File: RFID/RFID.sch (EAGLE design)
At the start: 2 parts, among them IC1 ARDUINO_PRO_MICRO, IC2 RFID_SENSOR

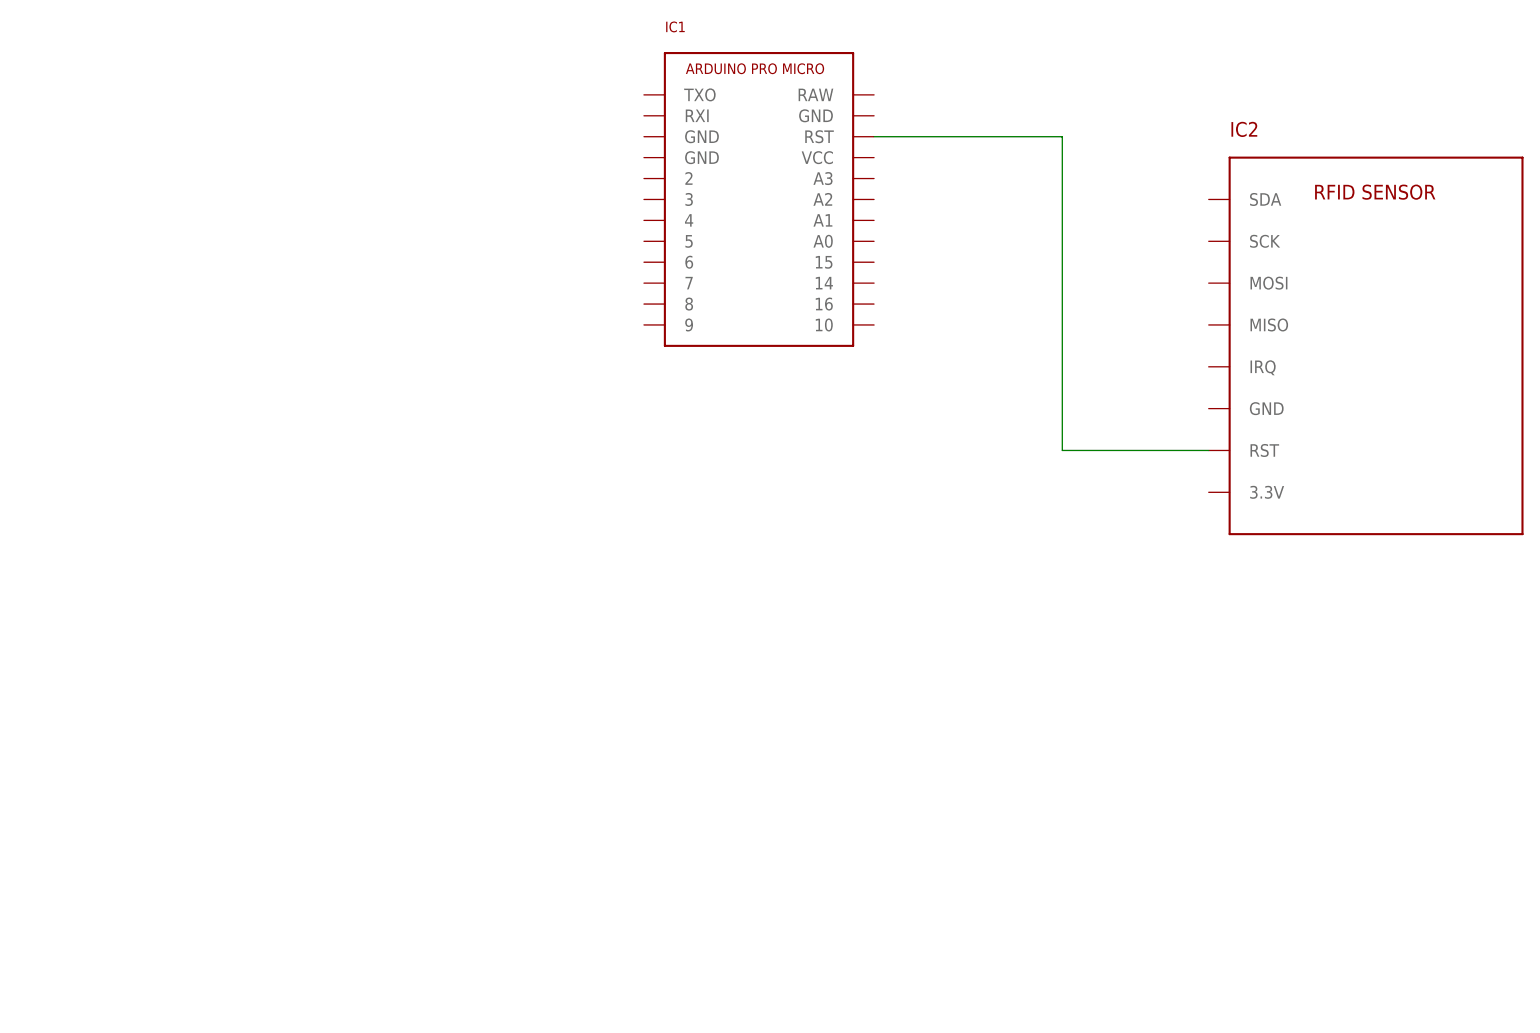
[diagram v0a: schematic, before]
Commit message: Remove old RFID board
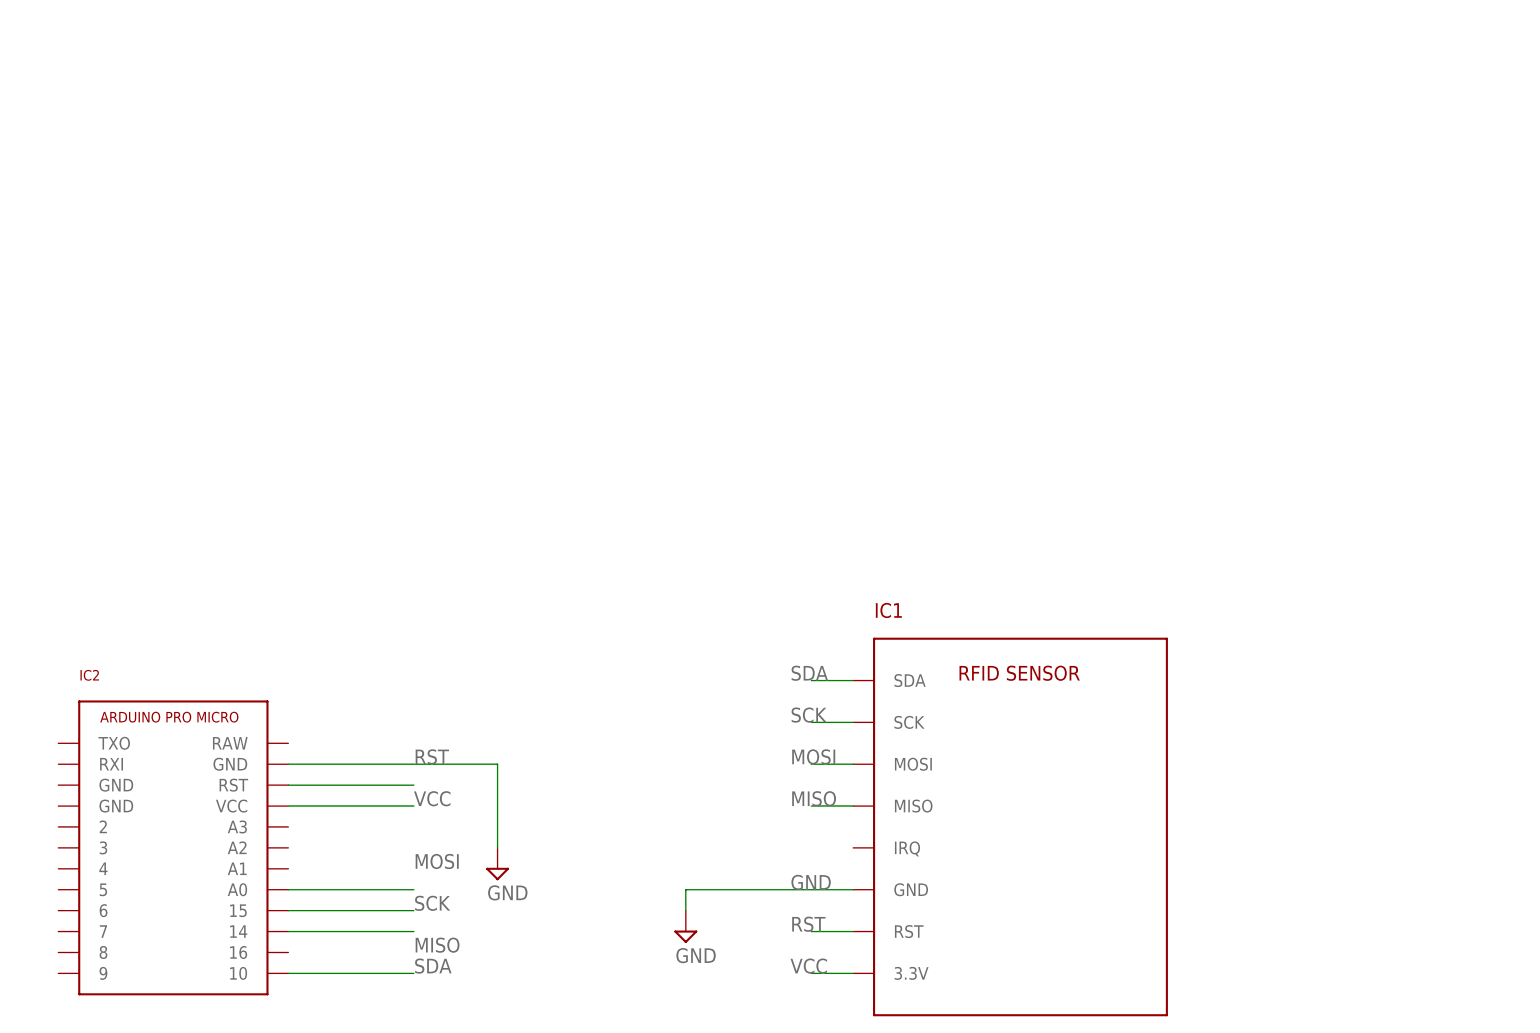
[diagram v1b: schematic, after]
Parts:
- IC1: value ARDUINO_PRO_MICRO -> RFID_SENSOR; device pie:ARDUINO_PRO_MICRO -> pie:RFID_SENSOR
- IC2: value RFID_SENSOR -> ARDUINO_PRO_MICRO; device pie:RFID_SENSOR -> pie:ARDUINO_PRO_MICRO
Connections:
- net N$1 renamed RST
- new net GND: IC1.GND, IC2.GND@2
- new net MISO: IC1.MISO, IC2.14
- new net MOSI: IC1.MOSI, IC2.A0
- new net SCK: IC1.SCK, IC2.15
- new net SDA: IC1.SDA, IC2.10
- new net VCC: IC1.3.3V, IC2.VCC
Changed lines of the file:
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@@
 <drawing>
 <settings>
-<setting alwaysvectorfont="yes"/>
+<setting alwaysvectorfont="no"/>
 <setting verticaltext="up"/>
 </settings>
@@
 </classes>
 <parts>
-<part name="FRAME1" library="pie" deviceset="FRAME_SCHEMATIC" device="">
-<attribute name="AUTHOR" value="Seiya Ono"/>
-<attribute name="REVISION" value="9B"/>
-</part>
-<part name="IC1" library="pie" deviceset="ARDUINO_PRO_MICRO" device=""/>
-<part name="IC2" library="pie" deviceset="RFID_SENSOR" device=""/>
+<part name="IC1" library="pie" deviceset="RFID_SENSOR" device=""/>
+<part name="IC2" library="pie" deviceset="ARDUINO_PRO_MICRO" device=""/>
+<part name="SUPPLY1" library="pie" deviceset="GND" device=""/>
+<part name="SUPPLY2" library="pie" deviceset="GND" device=""/>
 </parts>
 <sheets>
@@
 </plain>
 <instances>
-<instance part="FRAME1" gate="G$1" x="0" y="0">
-<attribute name="AUTHOR" x="0" y="0" size="1.778" layer="96" display="off"/>
-<attribute name="REVISION" x="0" y="0" size="1.778" layer="96" display="off"/>
-</instance>
-<instance part="FRAME1" gate="G$2" x="147.32" y="0"/>
-<instance part="IC1" gate="G$1" x="58.42" y="124.46"/>
-<instance part="IC2" gate="G$1" x="134.62" y="109.22"/>
+<instance part="IC1" gate="G$1" x="91.44" y="50.8"/>
+<instance part="IC2" gate="G$1" x="-12.7" y="45.72"/>
+<instance part="SUPPLY1" gate="GND" x="27.94" y="43.18"/>
+<instance part="SUPPLY2" gate="GND" x="50.8" y="35.56"/>
 </instances>
 <busses>
 </busses>
 <nets>
-<net name="N$1" class="0">
+<net name="VCC" class="0">
+<segment>
+<pinref part="IC2" gate="G$1" pin="VCC"/>
+<wire x1="2.54" y1="50.8" x2="17.78" y2="50.8" width="0.1524" layer="91"/>
+<label x="17.78" y="50.8" size="1.778" layer="95"/>
+</segment>
+<segment>
+<pinref part="IC1" gate="G$1" pin="3.3V"/>
+<wire x1="71.12" y1="30.48" x2="66.04" y2="30.48" width="0.1524" layer="91"/>
+<label x="63.5" y="30.48" size="1.778" layer="95"/>
+</segment>
+</net>
+<net name="RST" class="0">
 <segment>
 <pinref part="IC2" gate="G$1" pin="RST"/>
-<wire x1="114.3" y1="93.98" x2="96.52" y2="93.98" width="0.1524" layer="91"/>
-<wire x1="96.52" y1="93.98" x2="96.52" y2="132.08" width="0.1524" layer="91"/>
+<wire x1="2.54" y1="53.34" x2="17.78" y2="53.34" width="0.1524" layer="91"/>
+<label x="17.78" y="55.88" size="1.778" layer="95"/>
+</segment>
+<segment>
 <pinref part="IC1" gate="G$1" pin="RST"/>
-<wire x1="96.52" y1="132.08" x2="73.66" y2="132.08" width="0.1524" layer="91"/>
-</segment>
-</net>
+<wire x1="71.12" y1="35.56" x2="66.04" y2="35.56" width="0.1524" layer="91"/>
+<label x="63.5" y="35.56" size="1.778" layer="95"/>
+</segment>
+</net>
+<net name="GND" class="0">
+<segment>
+<pinref part="IC1" gate="G$1" pin="GND"/>
+<label x="63.5" y="40.64" size="1.778" layer="95"/>
+<wire x1="71.12" y1="40.64" x2="50.8" y2="40.64" width="0.1524" layer="91"/>
+<pinref part="SUPPLY2" gate="GND" pin="GND"/>
+<wire x1="50.8" y1="40.64" x2="50.8" y2="38.1" width="0.1524" layer="91"/>
+</segment>
+<segment>
+<pinref part="IC2" gate="G$1" pin="GND@2"/>
+<wire x1="2.54" y1="55.88" x2="27.94" y2="55.88" width="0.1524" layer="91"/>
+<wire x1="27.94" y1="55.88" x2="27.94" y2="45.72" width="0.1524" layer="91"/>
+<pinref part="SUPPLY1" gate="GND" pin="GND"/>
+</segment>
+</net>
+<net name="SDA" class="0">
+<segment>
+<pinref part="IC2" gate="G$1" pin="10"/>
+<wire x1="2.54" y1="30.48" x2="17.78" y2="30.48" width="0.1524" layer="91"/>
+<label x="17.78" y="30.48" size="1.778" layer="95"/>
+</segment>
+<segment>
+<pinref part="IC1" gate="G$1" pin="SDA"/>
+<wire x1="71.12" y1="66.04" x2="66.04" y2="66.04" width="0.1524" layer="91"/>
+<label x="63.5" y="66.04" size="1.778" layer="95"/>
+</segment>
+</net>
+<net name="MOSI" class="0">
+<segment>
+<pinref part="IC2" gate="G$1" pin="A0"/>
+<wire x1="2.54" y1="40.64" x2="17.78" y2="40.64" width="0.1524" layer="91"/>
+<label x="17.78" y="43.18" size="1.778" layer="95"/>
+</segment>
+<segment>
+<pinref part="IC1" gate="G$1" pin="MOSI"/>
+<wire x1="71.12" y1="55.88" x2="66.04" y2="55.88" width="0.1524" layer="91"/>
+<label x="63.5" y="55.88" size="1.778" layer="95"/>
+</segment>
+</net>
+<net name="MISO" class="0">
+<segment>
+<pinref part="IC2" gate="G$1" pin="14"/>
+<wire x1="2.54" y1="35.56" x2="17.78" y2="35.56" width="0.1524" layer="91"/>
+<label x="17.78" y="33.02" size="1.778" layer="95"/>
+</segment>
+<segment>
+<pinref part="IC1" gate="G$1" pin="MISO"/>
+<wire x1="71.12" y1="50.8" x2="66.04" y2="50.8" width="0.1524" layer="91"/>
+<label x="63.5" y="50.8" size="1.778" layer="95"/>
+</segment>
+</net>
+<net name="SCK" class="0">
+<segment>
+<pinref part="IC2" gate="G$1" pin="15"/>
+<wire x1="2.54" y1="38.1" x2="17.78" y2="38.1" width="0.1524" layer="91"/>
+<label x="17.78" y="38.1" size="1.778" layer="95"/>
+</segment>
+<segment>
+<pinref part="IC1" gate="G$1" pin="SCK"/>
+<wire x1="71.12" y1="60.96" x2="66.04" y2="60.96" width="0.1524" layer="91"/>
+<label x="63.5" y="60.96" size="1.778" layer="95"/>
+</segment>
+</net>

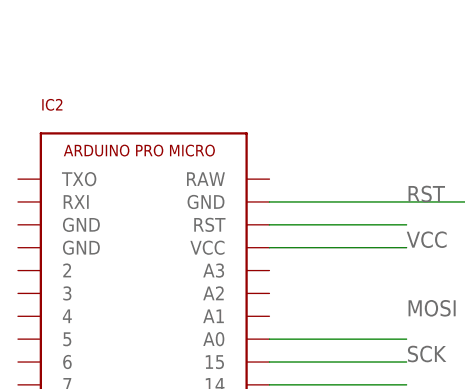
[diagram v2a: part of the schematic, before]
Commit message: Change RFID to be more space efficient
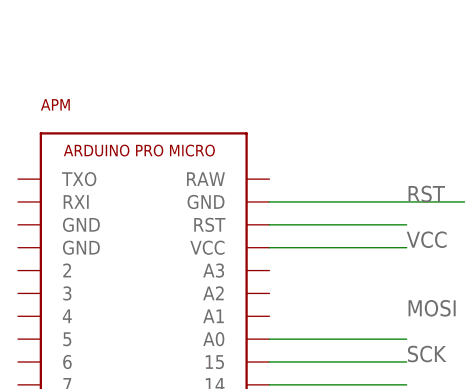
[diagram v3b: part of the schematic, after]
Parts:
- renumbered IC2 to APM
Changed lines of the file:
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@@
 <parts>
 <part name="IC1" library="pie" deviceset="RFID_SENSOR" device=""/>
-<part name="IC2" library="pie" deviceset="ARDUINO_PRO_MICRO" device=""/>
+<part name="APM" library="pie" deviceset="ARDUINO_PRO_MICRO" device=""/>
 <part name="SUPPLY1" library="pie" deviceset="GND" device=""/>
 <part name="SUPPLY2" library="pie" deviceset="GND" device=""/>
@@
 <instances>
 <instance part="IC1" gate="G$1" x="91.44" y="50.8"/>
-<instance part="IC2" gate="G$1" x="-12.7" y="45.72"/>
+<instance part="APM" gate="G$1" x="-12.7" y="45.72"/>
 <instance part="SUPPLY1" gate="GND" x="27.94" y="43.18"/>
 <instance part="SUPPLY2" gate="GND" x="50.8" y="35.56"/>
@@
 <net name="VCC" class="0">
 <segment>
-<pinref part="IC2" gate="G$1" pin="VCC"/>
+<pinref part="APM" gate="G$1" pin="VCC"/>
 <wire x1="2.54" y1="50.8" x2="17.78" y2="50.8" width="0.1524" layer="91"/>
 <label x="17.78" y="50.8" size="1.778" layer="95"/>
@@
 <net name="RST" class="0">
 <segment>
-<pinref part="IC2" gate="G$1" pin="RST"/>
+<pinref part="APM" gate="G$1" pin="RST"/>
 <wire x1="2.54" y1="53.34" x2="17.78" y2="53.34" width="0.1524" layer="91"/>
 <label x="17.78" y="55.88" size="1.778" layer="95"/>
@@
 </segment>
 <segment>
-<pinref part="IC2" gate="G$1" pin="GND@2"/>
+<pinref part="APM" gate="G$1" pin="GND@2"/>
 <wire x1="2.54" y1="55.88" x2="27.94" y2="55.88" width="0.1524" layer="91"/>
 <wire x1="27.94" y1="55.88" x2="27.94" y2="45.72" width="0.1524" layer="91"/>
@@
 <net name="SDA" class="0">
 <segment>
-<pinref part="IC2" gate="G$1" pin="10"/>
+<pinref part="APM" gate="G$1" pin="10"/>
 <wire x1="2.54" y1="30.48" x2="17.78" y2="30.48" width="0.1524" layer="91"/>
 <label x="17.78" y="30.48" size="1.778" layer="95"/>
@@
 <net name="MOSI" class="0">
 <segment>
-<pinref part="IC2" gate="G$1" pin="A0"/>
+<pinref part="APM" gate="G$1" pin="A0"/>
 <wire x1="2.54" y1="40.64" x2="17.78" y2="40.64" width="0.1524" layer="91"/>
 <label x="17.78" y="43.18" size="1.778" layer="95"/>
@@
 <net name="MISO" class="0">
 <segment>
-<pinref part="IC2" gate="G$1" pin="14"/>
+<pinref part="APM" gate="G$1" pin="14"/>
 <wire x1="2.54" y1="35.56" x2="17.78" y2="35.56" width="0.1524" layer="91"/>
 <label x="17.78" y="33.02" size="1.778" layer="95"/>
@@
 <net name="SCK" class="0">
 <segment>
-<pinref part="IC2" gate="G$1" pin="15"/>
+<pinref part="APM" gate="G$1" pin="15"/>
 <wire x1="2.54" y1="38.1" x2="17.78" y2="38.1" width="0.1524" layer="91"/>
 <label x="17.78" y="38.1" size="1.778" layer="95"/>

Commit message: Fix pins, change test
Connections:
- net MOSI: now also APM.16; no longer APM.A0
- net RST: now also APM.9; no longer APM.RST
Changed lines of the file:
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@@
 </classes>
 <parts>
-<part name="IC1" library="pie" deviceset="RFID_SENSOR" device=""/>
+<part name="IC1" library="pie" deviceset="RFID_SENSOR" device="" value="RFID_SENSOR"/>
 <part name="APM" library="pie" deviceset="ARDUINO_PRO_MICRO" device=""/>
 <part name="SUPPLY1" library="pie" deviceset="GND" device=""/>
@@
 <instances>
 <instance part="IC1" gate="G$1" x="91.44" y="50.8"/>
-<instance part="APM" gate="G$1" x="-12.7" y="45.72"/>
+<instance part="APM" gate="APM" x="-12.7" y="45.72"/>
 <instance part="SUPPLY1" gate="GND" x="27.94" y="43.18"/>
 <instance part="SUPPLY2" gate="GND" x="50.8" y="35.56"/>
@@
 <net name="VCC" class="0">
 <segment>
-<pinref part="APM" gate="G$1" pin="VCC"/>
+<pinref part="APM" gate="APM" pin="VCC"/>
 <wire x1="2.54" y1="50.8" x2="17.78" y2="50.8" width="0.1524" layer="91"/>
 <label x="17.78" y="50.8" size="1.778" layer="95"/>
@@
 <net name="RST" class="0">
 <segment>
-<pinref part="APM" gate="G$1" pin="RST"/>
-<wire x1="2.54" y1="53.34" x2="17.78" y2="53.34" width="0.1524" layer="91"/>
-<label x="17.78" y="55.88" size="1.778" layer="95"/>
-</segment>
-<segment>
 <pinref part="IC1" gate="G$1" pin="RST"/>
 <wire x1="71.12" y1="35.56" x2="66.04" y2="35.56" width="0.1524" layer="91"/>
 <label x="63.5" y="35.56" size="1.778" layer="95"/>
+</segment>
+<segment>
+<pinref part="APM" gate="APM" pin="9"/>
+<wire x1="-25.4" y1="30.48" x2="-30.48" y2="30.48" width="0.1524" layer="91"/>
+<label x="-30.48" y="30.48" size="1.778" layer="95"/>
 </segment>
 </net>
@@
 </segment>
 <segment>
-<pinref part="APM" gate="G$1" pin="GND@2"/>
+<pinref part="APM" gate="APM" pin="GND@2"/>
 <wire x1="2.54" y1="55.88" x2="27.94" y2="55.88" width="0.1524" layer="91"/>
 <wire x1="27.94" y1="55.88" x2="27.94" y2="45.72" width="0.1524" layer="91"/>
@@
 <net name="SDA" class="0">
 <segment>
-<pinref part="APM" gate="G$1" pin="10"/>
+<pinref part="APM" gate="APM" pin="10"/>
 <wire x1="2.54" y1="30.48" x2="17.78" y2="30.48" width="0.1524" layer="91"/>
 <label x="17.78" y="30.48" size="1.778" layer="95"/>
@@
 <net name="MOSI" class="0">
 <segment>
-<pinref part="APM" gate="G$1" pin="A0"/>
-<wire x1="2.54" y1="40.64" x2="17.78" y2="40.64" width="0.1524" layer="91"/>
-<label x="17.78" y="43.18" size="1.778" layer="95"/>
-</segment>
-<segment>
 <pinref part="IC1" gate="G$1" pin="MOSI"/>
 <wire x1="71.12" y1="55.88" x2="66.04" y2="55.88" width="0.1524" layer="91"/>
 <label x="63.5" y="55.88" size="1.778" layer="95"/>
 </segment>
+<segment>
+<pinref part="APM" gate="APM" pin="16"/>
+<wire x1="2.54" y1="33.02" x2="17.78" y2="33.02" width="0.1524" layer="91"/>
+<label x="17.78" y="33.02" size="1.778" layer="95"/>
+</segment>
 </net>
 <net name="MISO" class="0">
 <segment>
-<pinref part="APM" gate="G$1" pin="14"/>
+<pinref part="APM" gate="APM" pin="14"/>
 <wire x1="2.54" y1="35.56" x2="17.78" y2="35.56" width="0.1524" layer="91"/>
-<label x="17.78" y="33.02" size="1.778" layer="95"/>
+<label x="17.78" y="35.56" size="1.778" layer="95"/>
 </segment>
 <segment>
@@
 <net name="SCK" class="0">
 <segment>
-<pinref part="APM" gate="G$1" pin="15"/>
+<pinref part="APM" gate="APM" pin="15"/>
 <wire x1="2.54" y1="38.1" x2="17.78" y2="38.1" width="0.1524" layer="91"/>
 <label x="17.78" y="38.1" size="1.778" layer="95"/>
